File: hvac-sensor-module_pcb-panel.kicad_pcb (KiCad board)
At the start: 2 copper layers, 180 x 106 mm, 583 parts, among them J1 Conn_01x04, J2 Sensor, J3 Sensor, P1 Debug, Q1 RSS060P05FRATB, SW1 SW_PUSH, SW2 SW_PUSH, SW3 SW_PUSH, U1 LMR16006, U2 HDC1080, U3 STM32F072C8Tx, U5 TCAN334

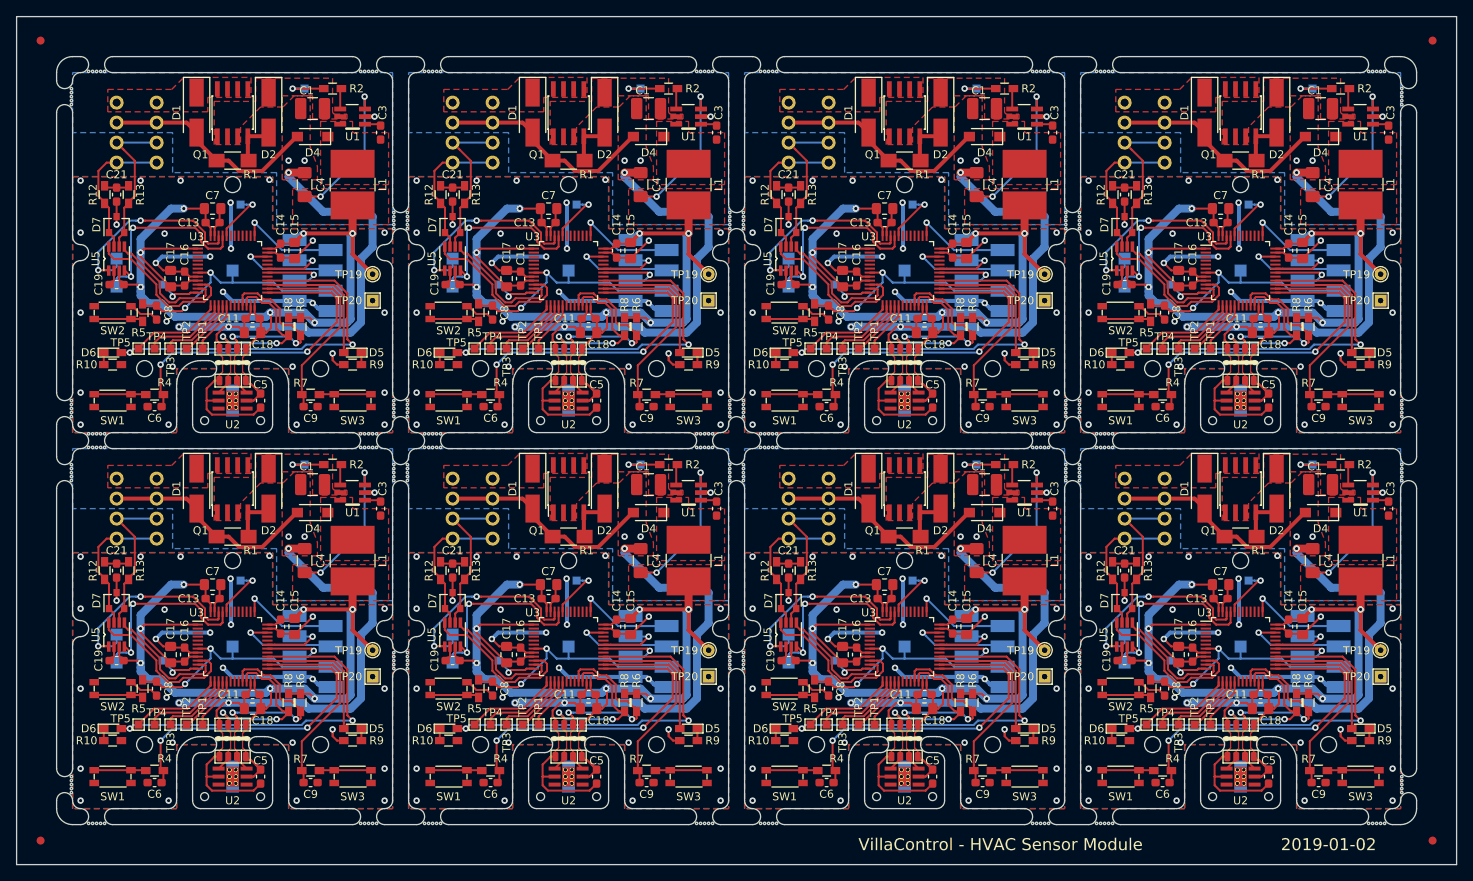
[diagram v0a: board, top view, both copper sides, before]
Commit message: Add some logos to PCB and update panel.
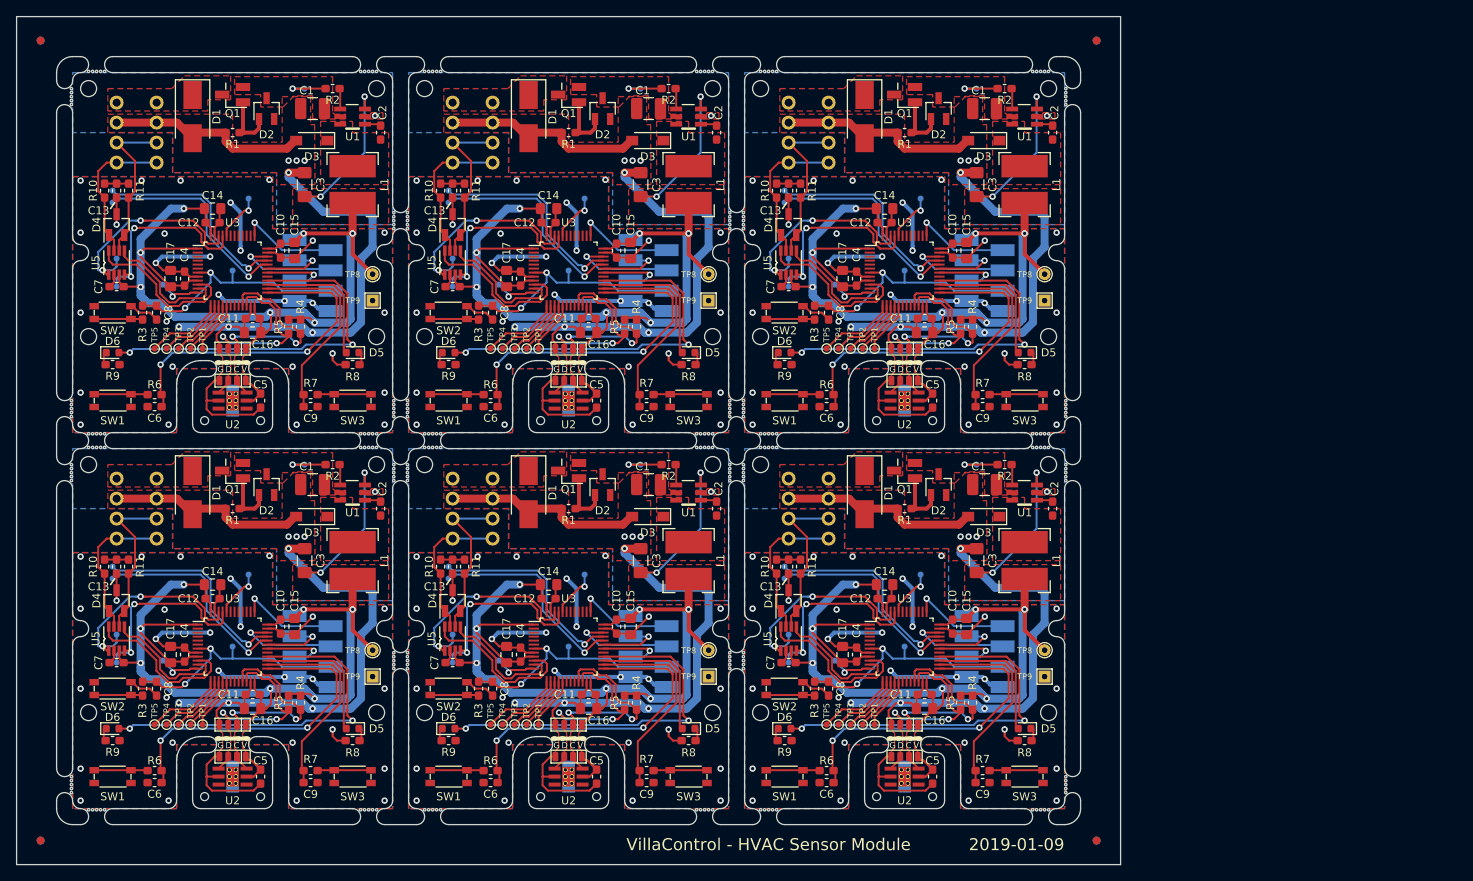
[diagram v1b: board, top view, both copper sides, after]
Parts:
- removed the C1 at (206.0, 101.5)
- removed the C1 at (206.0, 54.5)
- removed the C11 at (198.5, 127.8)
- removed the C11 at (198.5, 80.8)
- removed the C13 at (193.5, 115.8)
- removed the C13 at (193.5, 68.8)
- removed the C13 at (151.5, 115.8)
- removed the C13 at (151.5, 68.8)
- removed the C13 at (109.5, 115.8)
- removed the C13 at (109.5, 68.8)
- removed the C13 at (67.5, 115.8)
- removed the C13 at (67.5, 68.8)
- removed the C14 at (202.0, 119.2)
- removed the C14 at (202.0, 72.2)
- removed the C14 at (160.0, 119.2)
- removed the C14 at (160.0, 72.2)
- removed the C14 at (118.0, 119.2)
- removed the C14 at (118.0, 72.2)
- removed the C14 at (76.0, 119.2)
- removed the C14 at (76.0, 72.2)
- removed the C15 at (203.8, 119.2)
- removed the C15 at (203.8, 72.2)
- removed the C16 at (190.0, 122.8)
- removed the C16 at (190.0, 75.8)
- removed the C16 at (148.0, 122.8)
- removed the C16 at (148.0, 75.8)
- removed the C16 at (106.0, 122.8)
- removed the C16 at (106.0, 75.8)
- removed the C16 at (64.0, 122.8)
- removed the C16 at (64.0, 75.8)
- removed the C17 at (188.2, 122.8)
- removed the C17 at (188.2, 75.8)
- removed C18 (x8): 4µ7, Capacitor_SMD:C_0805_2012Metric_Pad1.15x1.40mm_HandSolder
- removed C19 (x8): 100n, Capacitor_SMD:C_0603_1608Metric_Pad1.05x0.95mm_HandSolder
- removed C21 (x8): 4n7, Capacitor_SMD:C_0603_1608Metric_Pad1.05x0.95mm_HandSolder
- removed the C3 at (214.5, 104.5)
- removed the C3 at (214.5, 57.5)
- removed the C3 at (172.5, 104.5)
- removed the C3 at (172.5, 57.5)
- removed the C3 at (130.5, 104.5)
- removed the C3 at (130.5, 57.5)
- removed the C3 at (88.5, 104.5)
- removed the C3 at (88.5, 57.5)
- removed the C4 at (205.0, 111.0)
- removed the C4 at (205.0, 64.0)
- removed the C4 at (163.0, 111.0)
- removed the C4 at (163.0, 64.0)
- removed the C4 at (121.0, 111.0)
- removed the C4 at (121.0, 64.0)
- removed the C4 at (79.0, 111.0)
- removed the C4 at (79.0, 64.0)
- removed the C5 at (199.5, 138.0)
- removed the C5 at (199.5, 91.0)
- removed the C6 at (186.2, 138.8)
- removed the C6 at (186.2, 91.8)
- removed the C7 at (193.5, 114.0)
- removed the C7 at (193.5, 67.0)
- removed the C7 at (151.5, 114.0)
- removed the C7 at (151.5, 67.0)
- removed the C7 at (109.5, 114.0)
- removed the C7 at (109.5, 67.0)
- removed the C7 at (67.5, 114.0)
- removed the C7 at (67.5, 67.0)
- removed the C8 at (186.5, 127.0)
- removed the C8 at (186.5, 80.0)
- removed the C9 at (205.8, 138.8)
- removed the C9 at (205.8, 91.8)
- removed the D1 at (191.5, 102.0)
- removed the D1 at (191.5, 55.0)
- removed the D1 at (149.5, 102.0)
- removed the D1 at (149.5, 55.0)
- removed the D1 at (107.5, 102.0)
- removed the D1 at (107.5, 55.0)
- removed the D1 at (65.5, 102.0)
- removed the D1 at (65.5, 55.0)
- removed the D2 at (200.5, 102.0)
- removed the D2 at (200.5, 55.0)
- removed the D2 at (158.5, 102.0)
- removed the D2 at (158.5, 55.0)
- removed the D2 at (116.5, 102.0)
- removed the D2 at (116.5, 55.0)
- removed the D2 at (74.5, 102.0)
- removed the D2 at (74.5, 55.0)
- removed the D4 at (206.0, 105.0)
- removed the D4 at (206.0, 58.0)
- removed the D4 at (164.0, 105.0)
- removed the D4 at (164.0, 58.0)
- removed the D4 at (122.0, 105.0)
- removed the D4 at (122.0, 58.0)
- removed the D4 at (80.0, 105.0)
- removed the D4 at (80.0, 58.0)
- removed the D5 at (211.0, 132.0)
- removed the D5 at (211.0, 85.0)
- removed the D5 at (169.0, 132.0)
- removed the D5 at (169.0, 85.0)
- removed the D5 at (127.0, 132.0)
- removed the D5 at (127.0, 85.0)
- removed the D5 at (85.0, 132.0)
- removed the D5 at (85.0, 85.0)
- removed the D6 at (181.0, 132.0)
- removed the D6 at (181.0, 85.0)
- removed the D6 at (139.0, 132.0)
- removed the D6 at (139.0, 85.0)
- removed the D6 at (97.0, 132.0)
- removed the D6 at (97.0, 85.0)
- removed the D6 at (55.0, 132.0)
- removed the D6 at (55.0, 85.0)
- removed D7 (x8): NUP2105L, TO_SOT_Packages_SMD:SOT-23
- removed the J1 at (184.0, 104.5)
- removed the J1 at (184.0, 57.5)
- removed the J2 at (196.0, 131.5)
- removed the J2 at (196.0, 84.5)
- removed the J3 at (196.0, 135.5)
- removed the J3 at (196.0, 88.5)
- removed the L1 at (211.0, 111.0)
- removed the L1 at (211.0, 64.0)
- removed the L1 at (169.0, 111.0)
- removed the L1 at (169.0, 64.0)
- removed the L1 at (127.0, 111.0)
- removed the L1 at (127.0, 64.0)
- removed the L1 at (85.0, 111.0)
- removed the L1 at (85.0, 64.0)
- removed the P1 at (206.0, 123.0)
- removed the P1 at (206.0, 76.0)
- removed the Q1 at (196.0, 102.0)
- removed the Q1 at (196.0, 55.0)
- removed the Q1 at (154.0, 102.0)
- removed the Q1 at (154.0, 55.0)
- removed the Q1 at (112.0, 102.0)
- removed the Q1 at (112.0, 55.0)
- removed the Q1 at (70.0, 102.0)
- removed the Q1 at (70.0, 55.0)
- removed the R1 at (196.0, 108.0)
- removed the R1 at (196.0, 61.0)
- removed the R1 at (154.0, 108.0)
- removed the R1 at (154.0, 61.0)
- removed the R1 at (112.0, 108.0)
- removed the R1 at (112.0, 61.0)
- removed the R1 at (70.0, 108.0)
- removed the R1 at (70.0, 61.0)
- removed the R10 at (181.0, 133.5)
- removed the R10 at (181.0, 86.5)
- removed the R10 at (139.0, 133.5)
- removed the R10 at (139.0, 86.5)
- removed the R10 at (97.0, 133.5)
- removed the R10 at (97.0, 86.5)
- removed the R10 at (55.0, 133.5)
- removed the R10 at (55.0, 86.5)
- removed R12 (x8), R13 (x8): 60.4 1%, Resistors_SMD:R_0603_HandSoldering
- removed the R2 at (208.5, 99.0)
- removed the R2 at (208.5, 52.0)
- removed the R2 at (166.5, 99.0)
- removed the R2 at (166.5, 52.0)
- removed the R2 at (124.5, 99.0)
- removed the R2 at (124.5, 52.0)
- removed the R2 at (82.5, 99.0)
- removed the R2 at (82.5, 52.0)
- removed the R4 at (186.2, 137.2)
- removed the R4 at (186.2, 90.2)
- removed the R4 at (144.2, 137.2)
- removed the R4 at (144.2, 90.2)
- removed the R4 at (102.2, 137.2)
- removed the R4 at (102.2, 90.2)
- removed the R4 at (60.2, 137.2)
- removed the R4 at (60.2, 90.2)
- removed the R5 at (184.8, 127.0)
- removed the R5 at (184.8, 80.0)
- removed the R5 at (142.8, 127.0)
- removed the R5 at (142.8, 80.0)
- removed the R5 at (100.8, 127.0)
- removed the R5 at (100.8, 80.0)
- removed the R5 at (58.8, 127.0)
- removed the R5 at (58.8, 80.0)
- removed the R6 at (204.5, 128.8)
- removed the R6 at (204.5, 81.8)
- removed the R6 at (162.5, 128.8)
- removed the R6 at (162.5, 81.8)
- removed the R6 at (120.5, 128.8)
- removed the R6 at (120.5, 81.8)
- removed the R6 at (78.5, 128.8)
- removed the R6 at (78.5, 81.8)
- removed the R7 at (205.8, 137.2)
- removed the R7 at (205.8, 90.2)
- removed the R7 at (163.8, 137.2)
- removed the R7 at (163.8, 90.2)
- removed the R7 at (121.8, 137.2)
- removed the R7 at (121.8, 90.2)
- removed the R7 at (79.8, 137.2)
- removed the R7 at (79.8, 90.2)
- removed the R8 at (203.0, 128.8)
- removed the R8 at (203.0, 81.8)
- removed the R8 at (161.0, 128.8)
- removed the R8 at (161.0, 81.8)
- removed the R8 at (119.0, 128.8)
- removed the R8 at (119.0, 81.8)
- removed the R8 at (77.0, 128.8)
- removed the R8 at (77.0, 81.8)
- removed the R9 at (211.0, 133.5)
- removed the R9 at (211.0, 86.5)
- removed the R9 at (169.0, 133.5)
- removed the R9 at (169.0, 86.5)
- removed the R9 at (127.0, 133.5)
- removed the R9 at (127.0, 86.5)
- removed the R9 at (85.0, 133.5)
- removed the R9 at (85.0, 86.5)
- removed the REF** at (179.0, 96.0)
- removed the REF** at (175.0, 100.0)
- removed the REF** at (175.0, 92.0)
- removed the REF** at (171.0, 143.0)
- removed the REF** at (179.0, 143.0)
- removed the REF** at (175.0, 123.5)
- removed the REF** at (213.0, 49.0)
- removed the REF** at (179.0, 49.0)
- removed the REF** at (175.0, 68.5)
- removed the REF** at (196.0, 133.2)
- removed the REF** at (196.0, 86.2)
- removed the REF** at (199.5, 140.5)
- removed the REF** at (199.5, 93.5)
- removed the REF** at (192.5, 140.5)
- removed the REF** at (192.5, 93.5)
- removed the REF** at (196.0, 111.0)
- removed the REF** at (196.0, 64.0)
- removed the REF** at (154.0, 111.0)
- removed the REF** at (154.0, 64.0)
- removed the REF** at (112.0, 111.0)
- removed the REF** at (112.0, 64.0)
- removed the REF** at (70.0, 111.0)
- removed the REF** at (185.0, 134.0)
- removed the REF** at (185.0, 87.0)
- removed the REF** at (143.0, 134.0)
- removed the REF** at (143.0, 87.0)
- removed the REF** at (101.0, 134.0)
- removed the REF** at (101.0, 87.0)
- removed the REF** at (59.0, 134.0)
- removed the REF** at (207.0, 134.0)
- removed the REF** at (207.0, 87.0)
- removed the REF** at (165.0, 134.0)
- removed the REF** at (165.0, 87.0)
- removed the REF** at (123.0, 134.0)
- removed the REF** at (123.0, 87.0)
- removed the REF** at (81.0, 134.0)
- removed the REF** at (209.5, 138.5)
- removed the REF** at (209.5, 91.5)
- removed the REF** at (167.5, 138.5)
- removed the REF** at (167.5, 91.5)
- removed the REF** at (125.5, 138.5)
- removed the REF** at (125.5, 91.5)
- removed the REF** at (83.5, 138.5)
- removed the REF** at (83.5, 91.5)
- removed the REF** at (81.0, 87.0)
- removed the REF** at (59.0, 87.0)
- removed the REF** at (70.0, 64.0)
- removed the SW1 at (181.0, 138.0)
- removed the SW1 at (181.0, 91.0)
- removed the SW2 at (181.0, 127.0)
- removed the SW2 at (181.0, 80.0)
- removed the SW3 at (211.0, 138.0)
- removed the SW3 at (211.0, 91.0)
- removed the TP1 at (192.2, 131.5)
- removed the TP1 at (192.2, 84.5)
- removed the TP1 at (150.2, 131.5)
- removed the TP1 at (150.2, 84.5)
- removed the TP1 at (108.2, 131.5)
- removed the TP1 at (108.2, 84.5)
- removed the TP1 at (66.2, 131.5)
- removed the TP1 at (66.2, 84.5)
- removed the TP11 at (196.0, 121.8)
- removed the TP11 at (196.0, 74.8)
- removed the TP11 at (154.0, 121.8)
- removed the TP11 at (154.0, 74.8)
- removed the TP11 at (112.0, 121.8)
- removed the TP11 at (112.0, 74.8)
- removed the TP11 at (70.0, 121.8)
- removed the TP11 at (70.0, 74.8)
- removed the TP14 at (181.5, 120.2)
- removed the TP14 at (181.5, 73.2)
- removed the TP14 at (139.5, 120.2)
- removed the TP14 at (139.5, 73.2)
- removed the TP14 at (97.5, 120.2)
- removed the TP14 at (97.5, 73.2)
- removed the TP14 at (55.5, 120.2)
- removed the TP14 at (55.5, 73.2)
- removed the TP15 at (181.5, 123.8)
- removed the TP15 at (181.5, 76.8)
- removed the TP15 at (139.5, 123.8)
- removed the TP15 at (139.5, 76.8)
- removed the TP15 at (97.5, 123.8)
- removed the TP15 at (97.5, 76.8)
- removed the TP15 at (55.5, 123.8)
- removed the TP15 at (55.5, 76.8)
- removed TP18 (x8): VINC, TestPoint:TestPoint_Pad_1.0x1.0mm
- removed TP19 (x8): 3.3V, TestPoint:TestPoint_THTPad_D1.5mm_Drill0.7mm
- removed the TP2 at (190.2, 131.5)
- removed the TP2 at (190.2, 84.5)
- removed the TP2 at (148.2, 131.5)
- removed the TP2 at (148.2, 84.5)
- removed the TP2 at (106.2, 131.5)
- removed the TP2 at (106.2, 84.5)
- removed the TP2 at (64.2, 131.5)
- removed the TP2 at (64.2, 84.5)
- removed TP20 (x8): GND, TestPoint:TestPoint_THTPad_1.5x1.5mm_Drill0.7mm
- removed TP21 (x8): BOOT0, TestPoint:TestPoint_Pad_1.0x1.0mm
- removed the TP3 at (188.2, 131.5)
- removed the TP3 at (188.2, 84.5)
- removed the TP3 at (146.2, 131.5)
- removed the TP3 at (146.2, 84.5)
- removed the TP3 at (104.2, 131.5)
- removed the TP3 at (104.2, 84.5)
- removed the TP3 at (62.2, 131.5)
- removed the TP3 at (62.2, 84.5)
- removed the TP4 at (186.2, 131.5)
- removed the TP4 at (186.2, 84.5)
- removed the TP4 at (144.2, 131.5)
- removed the TP4 at (144.2, 84.5)
- removed the TP4 at (102.2, 131.5)
- removed the TP4 at (102.2, 84.5)
- removed the TP4 at (60.2, 131.5)
- removed the TP4 at (60.2, 84.5)
- removed the TP5 at (184.2, 131.5)
- removed the TP5 at (184.2, 84.5)
- removed the TP5 at (142.2, 131.5)
- removed the TP5 at (142.2, 84.5)
- removed the TP5 at (100.2, 131.5)
- removed the TP5 at (100.2, 84.5)
- removed the TP5 at (58.2, 131.5)
- removed the TP5 at (58.2, 84.5)
- removed the TP6 at (187.2, 123.5)
- removed the TP6 at (187.2, 76.5)
- removed the TP6 at (145.2, 123.5)
- removed the TP6 at (145.2, 76.5)
- removed the TP6 at (103.2, 123.5)
- removed the TP6 at (103.2, 76.5)
- removed the TP6 at (61.2, 123.5)
- removed the TP6 at (61.2, 76.5)
- removed the U1 at (211.0, 102.5)
- removed the U1 at (211.0, 55.5)
- removed the U2 at (196.0, 138.0)
- removed the U2 at (196.0, 91.0)
- removed the U3 at (196.0, 121.8)
- removed the U3 at (196.0, 74.8)
- removed the U3 at (154.0, 121.8)
- removed the U3 at (154.0, 74.8)
- removed the U3 at (112.0, 121.8)
- removed the U3 at (112.0, 74.8)
- removed the U3 at (70.0, 121.8)
- removed the U3 at (70.0, 74.8)
- removed the U5 at (181.5, 120.2)
- removed the U5 at (181.5, 73.2)
- removed the U5 at (139.5, 120.2)
- removed the U5 at (139.5, 73.2)
- removed the U5 at (97.5, 120.2)
- removed the U5 at (97.5, 73.2)
- removed the U5 at (55.5, 120.2)
- removed the U5 at (55.5, 73.2)
- added C10: 100n, Capacitor_SMD:C_0603_1608Metric_Pad1.05x0.95mm_HandSolder, F.Cu at (160.0, 119.2)
- added C10: 100n, Capacitor_SMD:C_0603_1608Metric_Pad1.05x0.95mm_HandSolder, F.Cu at (160.0, 72.2)
- added C10: 100n, Capacitor_SMD:C_0603_1608Metric_Pad1.05x0.95mm_HandSolder, F.Cu at (76.0, 72.2)
- added C10: 100n, Capacitor_SMD:C_0603_1608Metric_Pad1.05x0.95mm_HandSolder, F.Cu at (118.0, 72.2)
- added C10: 100n, Capacitor_SMD:C_0603_1608Metric_Pad1.05x0.95mm_HandSolder, F.Cu at (76.0, 119.2)
- added C10: 100n, Capacitor_SMD:C_0603_1608Metric_Pad1.05x0.95mm_HandSolder, F.Cu at (118.0, 119.2)
- added C12: 100n, Capacitor_SMD:C_0603_1608Metric_Pad1.05x0.95mm_HandSolder, F.Cu at (151.5, 115.8)
- added C12: 100n, Capacitor_SMD:C_0603_1608Metric_Pad1.05x0.95mm_HandSolder, F.Cu at (151.5, 68.8)
- added C12: 100n, Capacitor_SMD:C_0603_1608Metric_Pad1.05x0.95mm_HandSolder, F.Cu at (67.5, 68.8)
- added C12: 100n, Capacitor_SMD:C_0603_1608Metric_Pad1.05x0.95mm_HandSolder, F.Cu at (109.5, 68.8)
- added C12: 100n, Capacitor_SMD:C_0603_1608Metric_Pad1.05x0.95mm_HandSolder, F.Cu at (67.5, 115.8)
- added C12: 100n, Capacitor_SMD:C_0603_1608Metric_Pad1.05x0.95mm_HandSolder, F.Cu at (109.5, 115.8)
- added C13: 4n7, Capacitor_SMD:C_0603_1608Metric_Pad1.05x0.95mm_HandSolder, F.Cu at (139.5, 111.8)
- added C13: 4n7, Capacitor_SMD:C_0603_1608Metric_Pad1.05x0.95mm_HandSolder, F.Cu at (139.5, 64.8)
- added C13: 4n7, Capacitor_SMD:C_0603_1608Metric_Pad1.05x0.95mm_HandSolder, F.Cu at (55.5, 64.8)
- added C13: 4n7, Capacitor_SMD:C_0603_1608Metric_Pad1.05x0.95mm_HandSolder, F.Cu at (97.5, 64.8)
- added C13: 4n7, Capacitor_SMD:C_0603_1608Metric_Pad1.05x0.95mm_HandSolder, F.Cu at (55.5, 111.8)
- added C13: 4n7, Capacitor_SMD:C_0603_1608Metric_Pad1.05x0.95mm_HandSolder, F.Cu at (97.5, 111.8)
- added C14: 4µ7, Capacitor_SMD:C_0805_2012Metric_Pad1.15x1.40mm_HandSolder, F.Cu at (151.5, 114.0)
- added C14: 4µ7, Capacitor_SMD:C_0805_2012Metric_Pad1.15x1.40mm_HandSolder, F.Cu at (151.5, 67.0)
- added C14: 4µ7, Capacitor_SMD:C_0805_2012Metric_Pad1.15x1.40mm_HandSolder, F.Cu at (67.5, 67.0)
- added C14: 4µ7, Capacitor_SMD:C_0805_2012Metric_Pad1.15x1.40mm_HandSolder, F.Cu at (109.5, 67.0)
- added C14: 4µ7, Capacitor_SMD:C_0805_2012Metric_Pad1.15x1.40mm_HandSolder, F.Cu at (67.5, 114.0)
- added C14: 4µ7, Capacitor_SMD:C_0805_2012Metric_Pad1.15x1.40mm_HandSolder, F.Cu at (109.5, 114.0)
- added C16: 4µ7, Capacitor_SMD:C_0805_2012Metric_Pad1.15x1.40mm_HandSolder, F.Cu at (156.5, 129.5)
- added C16: 4µ7, Capacitor_SMD:C_0805_2012Metric_Pad1.15x1.40mm_HandSolder, F.Cu at (156.5, 82.5)
- added C16: 4µ7, Capacitor_SMD:C_0805_2012Metric_Pad1.15x1.40mm_HandSolder, F.Cu at (72.5, 82.5)
- added C16: 4µ7, Capacitor_SMD:C_0805_2012Metric_Pad1.15x1.40mm_HandSolder, F.Cu at (114.5, 82.5)
- added C16: 4µ7, Capacitor_SMD:C_0805_2012Metric_Pad1.15x1.40mm_HandSolder, F.Cu at (72.5, 129.5)
- added C16: 4µ7, Capacitor_SMD:C_0805_2012Metric_Pad1.15x1.40mm_HandSolder, F.Cu at (114.5, 129.5)
- added C2: 100n, Capacitor_SMD:C_0603_1608Metric_Pad1.05x0.95mm_HandSolder, F.Cu at (172.5, 104.5)
- added C2: 100n, Capacitor_SMD:C_0603_1608Metric_Pad1.05x0.95mm_HandSolder, F.Cu at (172.5, 57.5)
- added C2: 100n, Capacitor_SMD:C_0603_1608Metric_Pad1.05x0.95mm_HandSolder, F.Cu at (88.5, 57.5)
- added C2: 100n, Capacitor_SMD:C_0603_1608Metric_Pad1.05x0.95mm_HandSolder, F.Cu at (130.5, 57.5)
- added C2: 100n, Capacitor_SMD:C_0603_1608Metric_Pad1.05x0.95mm_HandSolder, F.Cu at (88.5, 104.5)
- added C2: 100n, Capacitor_SMD:C_0603_1608Metric_Pad1.05x0.95mm_HandSolder, F.Cu at (130.5, 104.5)
- added C3: 22µF, Capacitor_SMD:C_1206_3216Metric_Pad1.42x1.75mm_HandSolder, F.Cu at (163.0, 111.0)
- added C3: 22µF, Capacitor_SMD:C_1206_3216Metric_Pad1.42x1.75mm_HandSolder, F.Cu at (163.0, 64.0)
- added C3: 22µF, Capacitor_SMD:C_1206_3216Metric_Pad1.42x1.75mm_HandSolder, F.Cu at (79.0, 64.0)
- added C3: 22µF, Capacitor_SMD:C_1206_3216Metric_Pad1.42x1.75mm_HandSolder, F.Cu at (121.0, 64.0)
- added C3: 22µF, Capacitor_SMD:C_1206_3216Metric_Pad1.42x1.75mm_HandSolder, F.Cu at (79.0, 111.0)
- added C3: 22µF, Capacitor_SMD:C_1206_3216Metric_Pad1.42x1.75mm_HandSolder, F.Cu at (121.0, 111.0)
- added C4: 100n, Capacitor_SMD:C_0603_1608Metric_Pad1.05x0.95mm_HandSolder, F.Cu at (148.0, 122.8)
- added C4: 100n, Capacitor_SMD:C_0603_1608Metric_Pad1.05x0.95mm_HandSolder, F.Cu at (148.0, 75.8)
- added C4: 100n, Capacitor_SMD:C_0603_1608Metric_Pad1.05x0.95mm_HandSolder, F.Cu at (64.0, 75.8)
- added C4: 100n, Capacitor_SMD:C_0603_1608Metric_Pad1.05x0.95mm_HandSolder, F.Cu at (106.0, 75.8)
- added C4: 100n, Capacitor_SMD:C_0603_1608Metric_Pad1.05x0.95mm_HandSolder, F.Cu at (64.0, 122.8)
- added C4: 100n, Capacitor_SMD:C_0603_1608Metric_Pad1.05x0.95mm_HandSolder, F.Cu at (106.0, 122.8)
- added C7: 100n, Capacitor_SMD:C_0603_1608Metric_Pad1.05x0.95mm_HandSolder, F.Cu at (139.5, 123.8)
- added C7: 100n, Capacitor_SMD:C_0603_1608Metric_Pad1.05x0.95mm_HandSolder, F.Cu at (139.5, 76.8)
- added C7: 100n, Capacitor_SMD:C_0603_1608Metric_Pad1.05x0.95mm_HandSolder, F.Cu at (55.5, 76.8)
- added C7: 100n, Capacitor_SMD:C_0603_1608Metric_Pad1.05x0.95mm_HandSolder, F.Cu at (97.5, 76.8)
- added C7: 100n, Capacitor_SMD:C_0603_1608Metric_Pad1.05x0.95mm_HandSolder, F.Cu at (55.5, 123.8)
- added C7: 100n, Capacitor_SMD:C_0603_1608Metric_Pad1.05x0.95mm_HandSolder, F.Cu at (97.5, 123.8)
- added D1: 40.2V, Diode_SMD:D_SMB_Handsoldering, F.Cu at (149.0, 102.5)
- added D1: 40.2V, Diode_SMD:D_SMB_Handsoldering, F.Cu at (149.0, 55.5)
- added D1: 40.2V, Diode_SMD:D_SMB_Handsoldering, F.Cu at (65.0, 55.5)
- added D1: 40.2V, Diode_SMD:D_SMB_Handsoldering, F.Cu at (107.0, 55.5)
- added D1: 40.2V, Diode_SMD:D_SMB_Handsoldering, F.Cu at (65.0, 102.5)
- added D1: 40.2V, Diode_SMD:D_SMB_Handsoldering, F.Cu at (107.0, 102.5)
- added D2: 10V, villa-control:D_SOT-23_ANK_Handsolder, F.Cu at (158.2, 101.5)
- added D2: 10V, villa-control:D_SOT-23_ANK_Handsolder, F.Cu at (158.2, 54.5)
- added D2: 10V, villa-control:D_SOT-23_ANK_Handsolder, F.Cu at (74.2, 54.5)
- added D2: 10V, villa-control:D_SOT-23_ANK_Handsolder, F.Cu at (116.2, 54.5)
- added D2: 10V, villa-control:D_SOT-23_ANK_Handsolder, F.Cu at (74.2, 101.5)
- added D2: 10V, villa-control:D_SOT-23_ANK_Handsolder, F.Cu at (116.2, 101.5)
- added D3: 50V Vrrm 1A, villa-control:D_SOD-123_Handsolder, F.Cu at (163.9, 105.5)
- added D3: 50V Vrrm 1A, villa-control:D_SOD-123_Handsolder, F.Cu at (163.9, 58.5)
- added D3: 50V Vrrm 1A, villa-control:D_SOD-123_Handsolder, F.Cu at (79.9, 58.5)
- added D3: 50V Vrrm 1A, villa-control:D_SOD-123_Handsolder, F.Cu at (121.9, 58.5)
- added D3: 50V Vrrm 1A, villa-control:D_SOD-123_Handsolder, F.Cu at (79.9, 105.5)
- added D3: 50V Vrrm 1A, villa-control:D_SOD-123_Handsolder, F.Cu at (121.9, 105.5)
- added D4: NUP2105L, villa-control:SOT-23_Handsoldering, F.Cu at (139.5, 116.0)
- added D4: NUP2105L, villa-control:SOT-23_Handsoldering, F.Cu at (139.5, 69.0)
- added D4: NUP2105L, villa-control:SOT-23_Handsoldering, F.Cu at (55.5, 69.0)
- added D4: NUP2105L, villa-control:SOT-23_Handsoldering, F.Cu at (97.5, 69.0)
- added D4: NUP2105L, villa-control:SOT-23_Handsoldering, F.Cu at (55.5, 116.0)
- added D4: NUP2105L, villa-control:SOT-23_Handsoldering, F.Cu at (97.5, 116.0)
- added D5: red, LED_SMD:LED_0603_1608Metric_Pad0.88x0.95mm_HandSolder, F.Cu at (169.0, 132.0)
- added D5: red, LED_SMD:LED_0603_1608Metric_Pad0.88x0.95mm_HandSolder, F.Cu at (169.0, 85.0)
- added D5: red, LED_SMD:LED_0603_1608Metric_Pad0.88x0.95mm_HandSolder, F.Cu at (85.0, 85.0)
- added D5: red, LED_SMD:LED_0603_1608Metric_Pad0.88x0.95mm_HandSolder, F.Cu at (127.0, 85.0)
- added D5: red, LED_SMD:LED_0603_1608Metric_Pad0.88x0.95mm_HandSolder, F.Cu at (85.0, 132.0)
- added D5: red, LED_SMD:LED_0603_1608Metric_Pad0.88x0.95mm_HandSolder, F.Cu at (127.0, 132.0)
- added D6: red, LED_SMD:LED_0603_1608Metric_Pad0.88x0.95mm_HandSolder, F.Cu at (139.0, 132.0)
- added D6: red, LED_SMD:LED_0603_1608Metric_Pad0.88x0.95mm_HandSolder, F.Cu at (139.0, 85.0)
- added D6: red, LED_SMD:LED_0603_1608Metric_Pad0.88x0.95mm_HandSolder, F.Cu at (55.0, 85.0)
- added D6: red, LED_SMD:LED_0603_1608Metric_Pad0.88x0.95mm_HandSolder, F.Cu at (97.0, 85.0)
- added D6: red, LED_SMD:LED_0603_1608Metric_Pad0.88x0.95mm_HandSolder, F.Cu at (55.0, 132.0)
- added D6: red, LED_SMD:LED_0603_1608Metric_Pad0.88x0.95mm_HandSolder, F.Cu at (97.0, 132.0)
- added L1: 27µH 220mΩ, villa-control:L_Bourns-SDR0604, F.Cu at (169.0, 111.0)
- added L1: 27µH 220mΩ, villa-control:L_Bourns-SDR0604, F.Cu at (169.0, 64.0)
- added L1: 27µH 220mΩ, villa-control:L_Bourns-SDR0604, F.Cu at (85.0, 64.0)
- added L1: 27µH 220mΩ, villa-control:L_Bourns-SDR0604, F.Cu at (127.0, 64.0)
- added L1: 27µH 220mΩ, villa-control:L_Bourns-SDR0604, F.Cu at (85.0, 111.0)
- added L1: 27µH 220mΩ, villa-control:L_Bourns-SDR0604, F.Cu at (127.0, 111.0)
- added Q1: FDN5618P, villa-control:SuperSOT-3_HandSoldering, F.Cu at (154.0, 99.8)
- added Q1: FDN5618P, villa-control:SuperSOT-3_HandSoldering, F.Cu at (154.0, 52.8)
- added Q1: FDN5618P, villa-control:SuperSOT-3_HandSoldering, F.Cu at (70.0, 52.8)
- added Q1: FDN5618P, villa-control:SuperSOT-3_HandSoldering, F.Cu at (112.0, 52.8)
- added Q1: FDN5618P, villa-control:SuperSOT-3_HandSoldering, F.Cu at (70.0, 99.8)
- added Q1: FDN5618P, villa-control:SuperSOT-3_HandSoldering, F.Cu at (112.0, 99.8)
- added R1: 100k, Resistor_SMD:R_0603_1608Metric_Pad1.05x0.95mm_HandSolder, F.Cu at (154.0, 104.5)
- added R1: 100k, Resistor_SMD:R_0603_1608Metric_Pad1.05x0.95mm_HandSolder, F.Cu at (154.0, 57.5)
- added R1: 100k, Resistor_SMD:R_0603_1608Metric_Pad1.05x0.95mm_HandSolder, F.Cu at (70.0, 57.5)
- added R1: 100k, Resistor_SMD:R_0603_1608Metric_Pad1.05x0.95mm_HandSolder, F.Cu at (112.0, 57.5)
- added R1: 100k, Resistor_SMD:R_0603_1608Metric_Pad1.05x0.95mm_HandSolder, F.Cu at (70.0, 104.5)
- added R1: 100k, Resistor_SMD:R_0603_1608Metric_Pad1.05x0.95mm_HandSolder, F.Cu at (112.0, 104.5)
- added R10: 60.4 1%, Resistor_SMD:R_0603_1608Metric_Pad1.05x0.95mm_HandSolder, F.Cu at (138.0, 111.8)
- added R10: 60.4 1%, Resistor_SMD:R_0603_1608Metric_Pad1.05x0.95mm_HandSolder, F.Cu at (138.0, 64.8)
- added R10: 60.4 1%, Resistor_SMD:R_0603_1608Metric_Pad1.05x0.95mm_HandSolder, F.Cu at (54.0, 64.8)
- added R10: 60.4 1%, Resistor_SMD:R_0603_1608Metric_Pad1.05x0.95mm_HandSolder, F.Cu at (96.0, 64.8)
- added R10: 60.4 1%, Resistor_SMD:R_0603_1608Metric_Pad1.05x0.95mm_HandSolder, F.Cu at (54.0, 111.8)
- added R10: 60.4 1%, Resistor_SMD:R_0603_1608Metric_Pad1.05x0.95mm_HandSolder, F.Cu at (96.0, 111.8)
- added R11: 60.4 1%, Resistor_SMD:R_0603_1608Metric_Pad1.05x0.95mm_HandSolder, F.Cu at (141.0, 111.8)
- added R11: 60.4 1%, Resistor_SMD:R_0603_1608Metric_Pad1.05x0.95mm_HandSolder, F.Cu at (141.0, 64.8)
- added R11: 60.4 1%, Resistor_SMD:R_0603_1608Metric_Pad1.05x0.95mm_HandSolder, F.Cu at (57.0, 64.8)
- added R11: 60.4 1%, Resistor_SMD:R_0603_1608Metric_Pad1.05x0.95mm_HandSolder, F.Cu at (99.0, 64.8)
- added R11: 60.4 1%, Resistor_SMD:R_0603_1608Metric_Pad1.05x0.95mm_HandSolder, F.Cu at (57.0, 111.8)
- added R11: 60.4 1%, Resistor_SMD:R_0603_1608Metric_Pad1.05x0.95mm_HandSolder, F.Cu at (99.0, 111.8)
- added R2: 100k, Resistor_SMD:R_0603_1608Metric_Pad1.05x0.95mm_HandSolder, F.Cu at (166.5, 99.0)
- added R2: 100k, Resistor_SMD:R_0603_1608Metric_Pad1.05x0.95mm_HandSolder, F.Cu at (166.5, 52.0)
- added R2: 100k, Resistor_SMD:R_0603_1608Metric_Pad1.05x0.95mm_HandSolder, F.Cu at (82.5, 52.0)
- added R2: 100k, Resistor_SMD:R_0603_1608Metric_Pad1.05x0.95mm_HandSolder, F.Cu at (124.5, 52.0)
- added R2: 100k, Resistor_SMD:R_0603_1608Metric_Pad1.05x0.95mm_HandSolder, F.Cu at (82.5, 99.0)
- added R2: 100k, Resistor_SMD:R_0603_1608Metric_Pad1.05x0.95mm_HandSolder, F.Cu at (124.5, 99.0)
- added R3: 220, Resistor_SMD:R_0603_1608Metric_Pad1.05x0.95mm_HandSolder, F.Cu at (142.8, 127.0)
- added R3: 220, Resistor_SMD:R_0603_1608Metric_Pad1.05x0.95mm_HandSolder, F.Cu at (142.8, 80.0)
- added R3: 220, Resistor_SMD:R_0603_1608Metric_Pad1.05x0.95mm_HandSolder, F.Cu at (58.8, 80.0)
- added R3: 220, Resistor_SMD:R_0603_1608Metric_Pad1.05x0.95mm_HandSolder, F.Cu at (100.8, 80.0)
- added R3: 220, Resistor_SMD:R_0603_1608Metric_Pad1.05x0.95mm_HandSolder, F.Cu at (58.8, 127.0)
- added R3: 220, Resistor_SMD:R_0603_1608Metric_Pad1.05x0.95mm_HandSolder, F.Cu at (100.8, 127.0)
- added R4: 3.3k, Resistor_SMD:R_0603_1608Metric_Pad1.05x0.95mm_HandSolder, F.Cu at (162.5, 128.8)
- added R4: 3.3k, Resistor_SMD:R_0603_1608Metric_Pad1.05x0.95mm_HandSolder, F.Cu at (162.5, 81.8)
- added R4: 3.3k, Resistor_SMD:R_0603_1608Metric_Pad1.05x0.95mm_HandSolder, F.Cu at (78.5, 81.8)
- added R4: 3.3k, Resistor_SMD:R_0603_1608Metric_Pad1.05x0.95mm_HandSolder, F.Cu at (120.5, 81.8)
- added R4: 3.3k, Resistor_SMD:R_0603_1608Metric_Pad1.05x0.95mm_HandSolder, F.Cu at (78.5, 128.8)
- added R4: 3.3k, Resistor_SMD:R_0603_1608Metric_Pad1.05x0.95mm_HandSolder, F.Cu at (120.5, 128.8)
- added R5: 3.3k, Resistor_SMD:R_0603_1608Metric_Pad1.05x0.95mm_HandSolder, F.Cu at (161.0, 128.8)
- added R5: 3.3k, Resistor_SMD:R_0603_1608Metric_Pad1.05x0.95mm_HandSolder, F.Cu at (161.0, 81.8)
- added R5: 3.3k, Resistor_SMD:R_0603_1608Metric_Pad1.05x0.95mm_HandSolder, F.Cu at (77.0, 81.8)
- added R5: 3.3k, Resistor_SMD:R_0603_1608Metric_Pad1.05x0.95mm_HandSolder, F.Cu at (119.0, 81.8)
- added R5: 3.3k, Resistor_SMD:R_0603_1608Metric_Pad1.05x0.95mm_HandSolder, F.Cu at (77.0, 128.8)
- added R5: 3.3k, Resistor_SMD:R_0603_1608Metric_Pad1.05x0.95mm_HandSolder, F.Cu at (119.0, 128.8)
- added R6: 3.3k, Resistor_SMD:R_0603_1608Metric_Pad1.05x0.95mm_HandSolder, F.Cu at (144.2, 137.2)
- added R6: 3.3k, Resistor_SMD:R_0603_1608Metric_Pad1.05x0.95mm_HandSolder, F.Cu at (144.2, 90.2)
- added R6: 3.3k, Resistor_SMD:R_0603_1608Metric_Pad1.05x0.95mm_HandSolder, F.Cu at (60.2, 90.2)
- added R6: 3.3k, Resistor_SMD:R_0603_1608Metric_Pad1.05x0.95mm_HandSolder, F.Cu at (102.2, 90.2)
- added R6: 3.3k, Resistor_SMD:R_0603_1608Metric_Pad1.05x0.95mm_HandSolder, F.Cu at (60.2, 137.2)
- added R6: 3.3k, Resistor_SMD:R_0603_1608Metric_Pad1.05x0.95mm_HandSolder, F.Cu at (102.2, 137.2)
- added R7: 3.3k, Resistor_SMD:R_0603_1608Metric_Pad1.05x0.95mm_HandSolder, F.Cu at (163.8, 137.2)
- added R7: 3.3k, Resistor_SMD:R_0603_1608Metric_Pad1.05x0.95mm_HandSolder, F.Cu at (163.8, 90.2)
- added R7: 3.3k, Resistor_SMD:R_0603_1608Metric_Pad1.05x0.95mm_HandSolder, F.Cu at (79.8, 90.2)
- added R7: 3.3k, Resistor_SMD:R_0603_1608Metric_Pad1.05x0.95mm_HandSolder, F.Cu at (121.8, 90.2)
- added R7: 3.3k, Resistor_SMD:R_0603_1608Metric_Pad1.05x0.95mm_HandSolder, F.Cu at (79.8, 137.2)
- added R7: 3.3k, Resistor_SMD:R_0603_1608Metric_Pad1.05x0.95mm_HandSolder, F.Cu at (121.8, 137.2)
- added R8: 220, Resistor_SMD:R_0603_1608Metric_Pad1.05x0.95mm_HandSolder, F.Cu at (169.0, 133.5)
- added R8: 220, Resistor_SMD:R_0603_1608Metric_Pad1.05x0.95mm_HandSolder, F.Cu at (169.0, 86.5)
- added R8: 220, Resistor_SMD:R_0603_1608Metric_Pad1.05x0.95mm_HandSolder, F.Cu at (85.0, 86.5)
- added R8: 220, Resistor_SMD:R_0603_1608Metric_Pad1.05x0.95mm_HandSolder, F.Cu at (127.0, 86.5)
- added R8: 220, Resistor_SMD:R_0603_1608Metric_Pad1.05x0.95mm_HandSolder, F.Cu at (85.0, 133.5)
- added R8: 220, Resistor_SMD:R_0603_1608Metric_Pad1.05x0.95mm_HandSolder, F.Cu at (127.0, 133.5)
- added R9: 220, Resistor_SMD:R_0603_1608Metric_Pad1.05x0.95mm_HandSolder, F.Cu at (139.0, 133.5)
- added R9: 220, Resistor_SMD:R_0603_1608Metric_Pad1.05x0.95mm_HandSolder, F.Cu at (139.0, 86.5)
- added R9: 220, Resistor_SMD:R_0603_1608Metric_Pad1.05x0.95mm_HandSolder, F.Cu at (55.0, 86.5)
- added R9: 220, Resistor_SMD:R_0603_1608Metric_Pad1.05x0.95mm_HandSolder, F.Cu at (97.0, 86.5)
- added R9: 220, Resistor_SMD:R_0603_1608Metric_Pad1.05x0.95mm_HandSolder, F.Cu at (55.0, 133.5)
- added R9: 220, Resistor_SMD:R_0603_1608Metric_Pad1.05x0.95mm_HandSolder, F.Cu at (97.0, 133.5)
- added REF**: Fiducial_1mm_Dia_2.54mm_Outer_CopperTop, Fiducial:Fiducial_1mm_Dia_2.54mm_Outer_CopperTop, B.Cu at (178.0, 146.0)
- added REF**: Fiducial_1mm_Dia_2.54mm_Outer_CopperTop, Fiducial:Fiducial_1mm_Dia_2.54mm_Outer_CopperTop, B.Cu at (178.0, 46.0)
- added REF**: Drill_2mm, villa-control:Drill_2mm, F.Cu at (136.0, 99.0)
- added REF**: Drill_2mm, villa-control:Drill_2mm, F.Cu at (136.0, 130.0)
- added REF**: OSHW-Logo2_7.3x6mm_SilkScreen, Symbol:OSHW-Logo2_7.3x6mm_SilkScreen, B.Cu at (167.4, 137.0)
- added REF**: Drill_2mm, villa-control:Drill_2mm, F.Cu at (172.0, 99.0)
- added REF**: KiCad-Logo2_6mm_SilkScreen, Symbol:KiCad-Logo2_6mm_SilkScreen, B.Cu at (140.7, 133.0)
- added REF**: Drill_2mm, villa-control:Drill_2mm, F.Cu at (172.0, 130.0)
- added REF**: Fiducial_1mm_Dia_2.54mm_Outer_CopperTop, Fiducial:Fiducial_1mm_Dia_2.54mm_Outer_CopperTop, B.Cu at (46.0, 46.0)
- added REF**: Drill_2mm, villa-control:Drill_2mm, F.Cu at (136.0, 52.0)
- added REF**: OSHW-Logo2_7.3x6mm_SilkScreen, Symbol:OSHW-Logo2_7.3x6mm_SilkScreen, B.Cu at (167.4, 90.0)
- added REF**: Drill_2mm, villa-control:Drill_2mm, F.Cu at (172.0, 52.0)
- added REF**: Drill_2mm, villa-control:Drill_2mm, F.Cu at (136.0, 83.0)
- added REF**: KiCad-Logo2_6mm_SilkScreen, Symbol:KiCad-Logo2_6mm_SilkScreen, B.Cu at (140.7, 86.0)
- added REF**: Drill_2mm, villa-control:Drill_2mm, F.Cu at (172.0, 83.0)
- added REF**: Fiducial_1mm_Dia_2.54mm_Outer_CopperTop, Fiducial:Fiducial_1mm_Dia_2.54mm_Outer_CopperTop, B.Cu at (46.0, 146.0)
- added REF**: KiCad-Logo2_6mm_SilkScreen, Symbol:KiCad-Logo2_6mm_SilkScreen, B.Cu at (56.6, 86.0)
- added REF**: Drill_2mm, villa-control:Drill_2mm, F.Cu at (88.0, 83.0)
- added REF**: Drill_2mm, villa-control:Drill_2mm, F.Cu at (52.0, 83.0)
- added REF**: Drill_2mm, villa-control:Drill_2mm, F.Cu at (52.0, 52.0)
- added REF**: Drill_2mm, villa-control:Drill_2mm, F.Cu at (88.0, 52.0)
- added REF**: OSHW-Logo2_7.3x6mm_SilkScreen, Symbol:OSHW-Logo2_7.3x6mm_SilkScreen, B.Cu at (83.5, 90.0)
- added REF**: KiCad-Logo2_6mm_SilkScreen, Symbol:KiCad-Logo2_6mm_SilkScreen, B.Cu at (98.7, 86.0)
- added REF**: Drill_2mm, villa-control:Drill_2mm, F.Cu at (130.0, 83.0)
- added REF**: Drill_2mm, villa-control:Drill_2mm, F.Cu at (94.0, 83.0)
- added REF**: Drill_2mm, villa-control:Drill_2mm, F.Cu at (94.0, 52.0)
- added REF**: Drill_2mm, villa-control:Drill_2mm, F.Cu at (130.0, 52.0)
- added REF**: OSHW-Logo2_7.3x6mm_SilkScreen, Symbol:OSHW-Logo2_7.3x6mm_SilkScreen, B.Cu at (125.5, 90.0)
- added REF**: KiCad-Logo2_6mm_SilkScreen, Symbol:KiCad-Logo2_6mm_SilkScreen, B.Cu at (56.6, 133.0)
- added REF**: Drill_2mm, villa-control:Drill_2mm, F.Cu at (88.0, 130.0)
- added REF**: Drill_2mm, villa-control:Drill_2mm, F.Cu at (52.0, 130.0)
- added REF**: Drill_2mm, villa-control:Drill_2mm, F.Cu at (52.0, 99.0)
- added REF**: Drill_2mm, villa-control:Drill_2mm, F.Cu at (88.0, 99.0)
- added REF**: OSHW-Logo2_7.3x6mm_SilkScreen, Symbol:OSHW-Logo2_7.3x6mm_SilkScreen, B.Cu at (83.5, 137.0)
- added REF**: KiCad-Logo2_6mm_SilkScreen, Symbol:KiCad-Logo2_6mm_SilkScreen, B.Cu at (98.7, 133.0)
- added REF**: Drill_2mm, villa-control:Drill_2mm, F.Cu at (130.0, 130.0)
- added REF**: Drill_2mm, villa-control:Drill_2mm, F.Cu at (94.0, 130.0)
- added REF**: Drill_2mm, villa-control:Drill_2mm, F.Cu at (94.0, 99.0)
- added REF**: Drill_2mm, villa-control:Drill_2mm, F.Cu at (130.0, 99.0)
- added REF**: OSHW-Logo2_7.3x6mm_SilkScreen, Symbol:OSHW-Logo2_7.3x6mm_SilkScreen, B.Cu at (125.5, 137.0)
- added TP1: PA7, villa-control:TestPoint_Pad_D0.75mm, F.Cu at (150.2, 131.5)
- added TP1: PA7, villa-control:TestPoint_Pad_D0.75mm, F.Cu at (150.2, 84.5)
- added TP1: PA7, villa-control:TestPoint_Pad_D0.75mm, F.Cu at (66.2, 84.5)
- added TP1: PA7, villa-control:TestPoint_Pad_D0.75mm, F.Cu at (108.2, 84.5)
- added TP1: PA7, villa-control:TestPoint_Pad_D0.75mm, F.Cu at (66.2, 131.5)
- added TP1: PA7, villa-control:TestPoint_Pad_D0.75mm, F.Cu at (108.2, 131.5)
- added TP10: NRST, villa-control:TestPoint_Pad_D0.75mm, B.Cu at (154.0, 121.8)
- added TP10: NRST, villa-control:TestPoint_Pad_D0.75mm, B.Cu at (154.0, 74.8)
- added TP10: NRST, villa-control:TestPoint_Pad_D0.75mm, B.Cu at (70.0, 74.8)
- added TP10: NRST, villa-control:TestPoint_Pad_D0.75mm, B.Cu at (112.0, 74.8)
- added TP10: NRST, villa-control:TestPoint_Pad_D0.75mm, B.Cu at (70.0, 121.8)
- added TP10: NRST, villa-control:TestPoint_Pad_D0.75mm, B.Cu at (112.0, 121.8)
- added TP11: BOOT0, villa-control:TestPoint_Pad_D0.75mm, B.Cu at (156.0, 112.8)
- added TP11: BOOT0, villa-control:TestPoint_Pad_D0.75mm, B.Cu at (156.0, 65.8)
- added TP11: BOOT0, villa-control:TestPoint_Pad_D0.75mm, B.Cu at (72.0, 65.8)
- added TP11: BOOT0, villa-control:TestPoint_Pad_D0.75mm, B.Cu at (114.0, 65.8)
- added TP11: BOOT0, villa-control:TestPoint_Pad_D0.75mm, B.Cu at (72.0, 112.8)
- added TP11: BOOT0, villa-control:TestPoint_Pad_D0.75mm, B.Cu at (114.0, 112.8)
- added TP12: CAN_TX, villa-control:TestPoint_Pad_D0.75mm, B.Cu at (139.5, 120.2)
- added TP12: CAN_TX, villa-control:TestPoint_Pad_D0.75mm, B.Cu at (139.5, 73.2)
- added TP12: CAN_TX, villa-control:TestPoint_Pad_D0.75mm, B.Cu at (55.5, 73.2)
- added TP12: CAN_TX, villa-control:TestPoint_Pad_D0.75mm, B.Cu at (97.5, 73.2)
- added TP12: CAN_TX, villa-control:TestPoint_Pad_D0.75mm, B.Cu at (55.5, 120.2)
- added TP12: CAN_TX, villa-control:TestPoint_Pad_D0.75mm, B.Cu at (97.5, 120.2)
- added TP13: CAN_RX, villa-control:TestPoint_Pad_D0.75mm, B.Cu at (139.5, 123.8)
- added TP13: CAN_RX, villa-control:TestPoint_Pad_D0.75mm, B.Cu at (139.5, 76.8)
- added TP13: CAN_RX, villa-control:TestPoint_Pad_D0.75mm, B.Cu at (55.5, 76.8)
- added TP13: CAN_RX, villa-control:TestPoint_Pad_D0.75mm, B.Cu at (97.5, 76.8)
- added TP13: CAN_RX, villa-control:TestPoint_Pad_D0.75mm, B.Cu at (55.5, 123.8)
- added TP13: CAN_RX, villa-control:TestPoint_Pad_D0.75mm, B.Cu at (97.5, 123.8)
- added TP14: USB_D-, villa-control:TestPoint_Pad_D0.75mm, B.Cu at (139.0, 113.2)
- added TP14: USB_D-, villa-control:TestPoint_Pad_D0.75mm, B.Cu at (139.0, 66.2)
- added TP14: USB_D-, villa-control:TestPoint_Pad_D0.75mm, B.Cu at (55.0, 66.2)
- added TP14: USB_D-, villa-control:TestPoint_Pad_D0.75mm, B.Cu at (97.0, 66.2)
- added TP14: USB_D-, villa-control:TestPoint_Pad_D0.75mm, B.Cu at (55.0, 113.2)
- added TP14: USB_D-, villa-control:TestPoint_Pad_D0.75mm, B.Cu at (97.0, 113.2)
- added TP15: USB_D+, villa-control:TestPoint_Pad_D0.75mm, B.Cu at (139.0, 111.8)
- added TP15: USB_D+, villa-control:TestPoint_Pad_D0.75mm, B.Cu at (139.0, 64.8)
- added TP15: USB_D+, villa-control:TestPoint_Pad_D0.75mm, B.Cu at (55.0, 64.8)
- added TP15: USB_D+, villa-control:TestPoint_Pad_D0.75mm, B.Cu at (97.0, 64.8)
- added TP15: USB_D+, villa-control:TestPoint_Pad_D0.75mm, B.Cu at (55.0, 111.8)
- added TP15: USB_D+, villa-control:TestPoint_Pad_D0.75mm, B.Cu at (97.0, 111.8)
- added TP2: PA6, villa-control:TestPoint_Pad_D0.75mm, F.Cu at (148.8, 131.5)
- added TP2: PA6, villa-control:TestPoint_Pad_D0.75mm, F.Cu at (148.8, 84.5)
- added TP2: PA6, villa-control:TestPoint_Pad_D0.75mm, F.Cu at (64.8, 84.5)
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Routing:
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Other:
- board size 180 x 106 mm -> 138 x 106 mm
- board text added: "2019-01-09"
- board text added: "C"
- board text added: "D"
- board text added: "G"
- board text added: "Rev. 1.0"
- board text added: "V"
- board text added: "VillaControl HVAC Sensor Module"
- board text removed: "2019-01-02"
- board text removed: "VillaControl HVAC Sensor Module 1.0"
